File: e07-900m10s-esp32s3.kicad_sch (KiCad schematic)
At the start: 21 parts, among them J1 Conn_01x08_Pin, J2 C3/S3mini, U1 E07-900M10S, U2 ESP32-S3-DevKitC

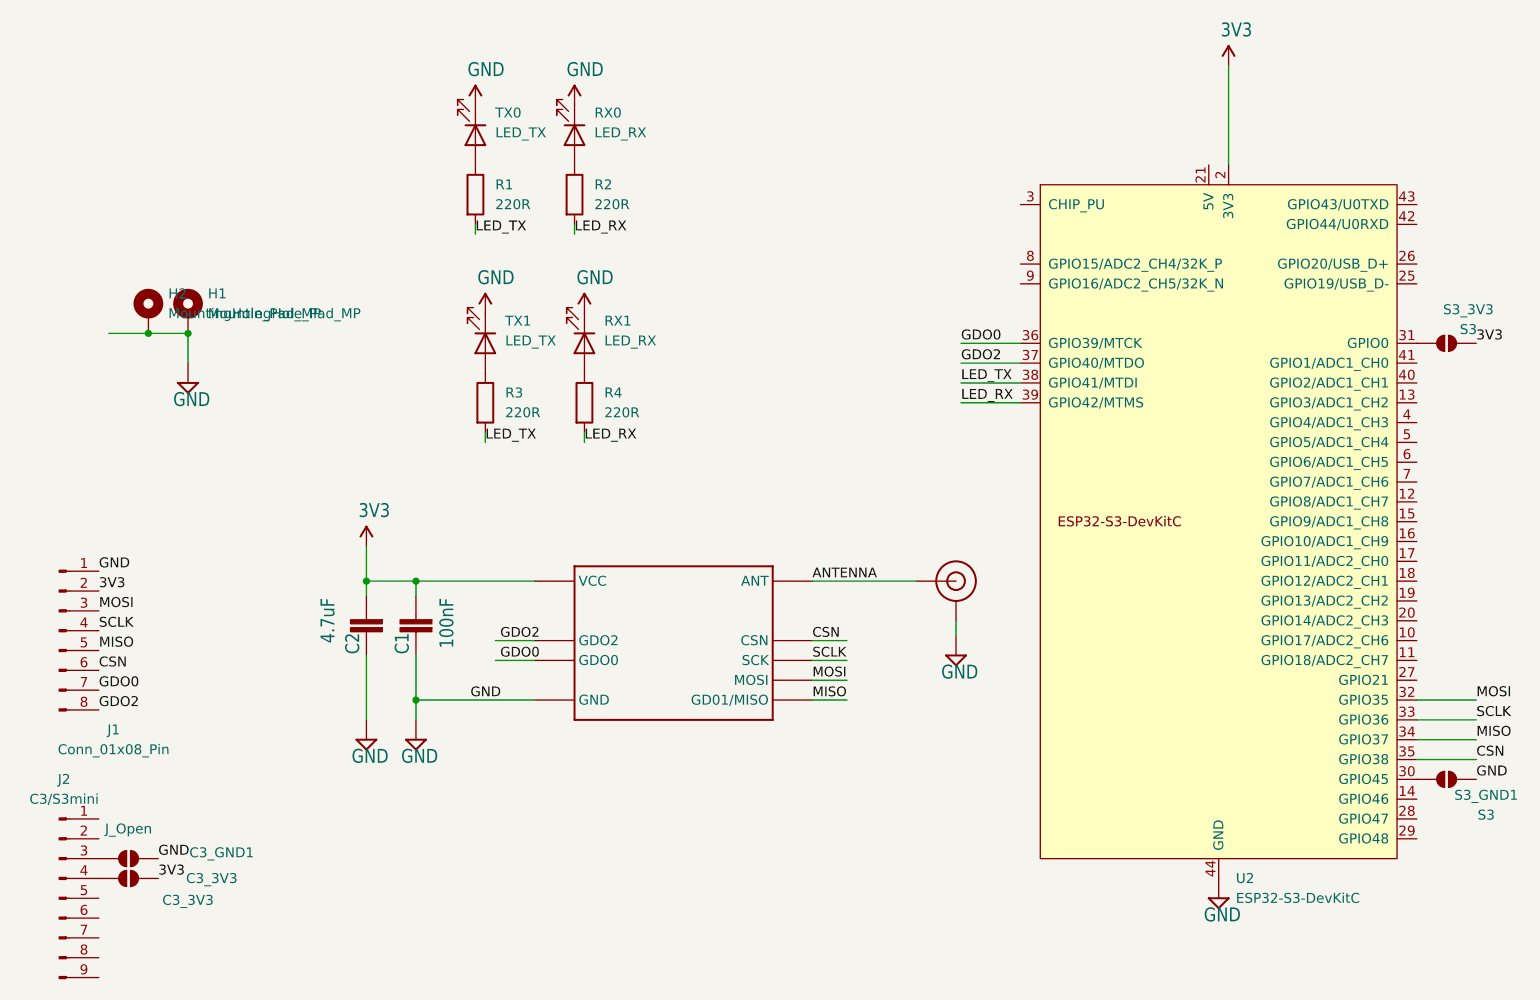
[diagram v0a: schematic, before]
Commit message: New version for JLC production
Header removed, PCB extended LED's switched for standard basic part and added MPN to components JLC solders.
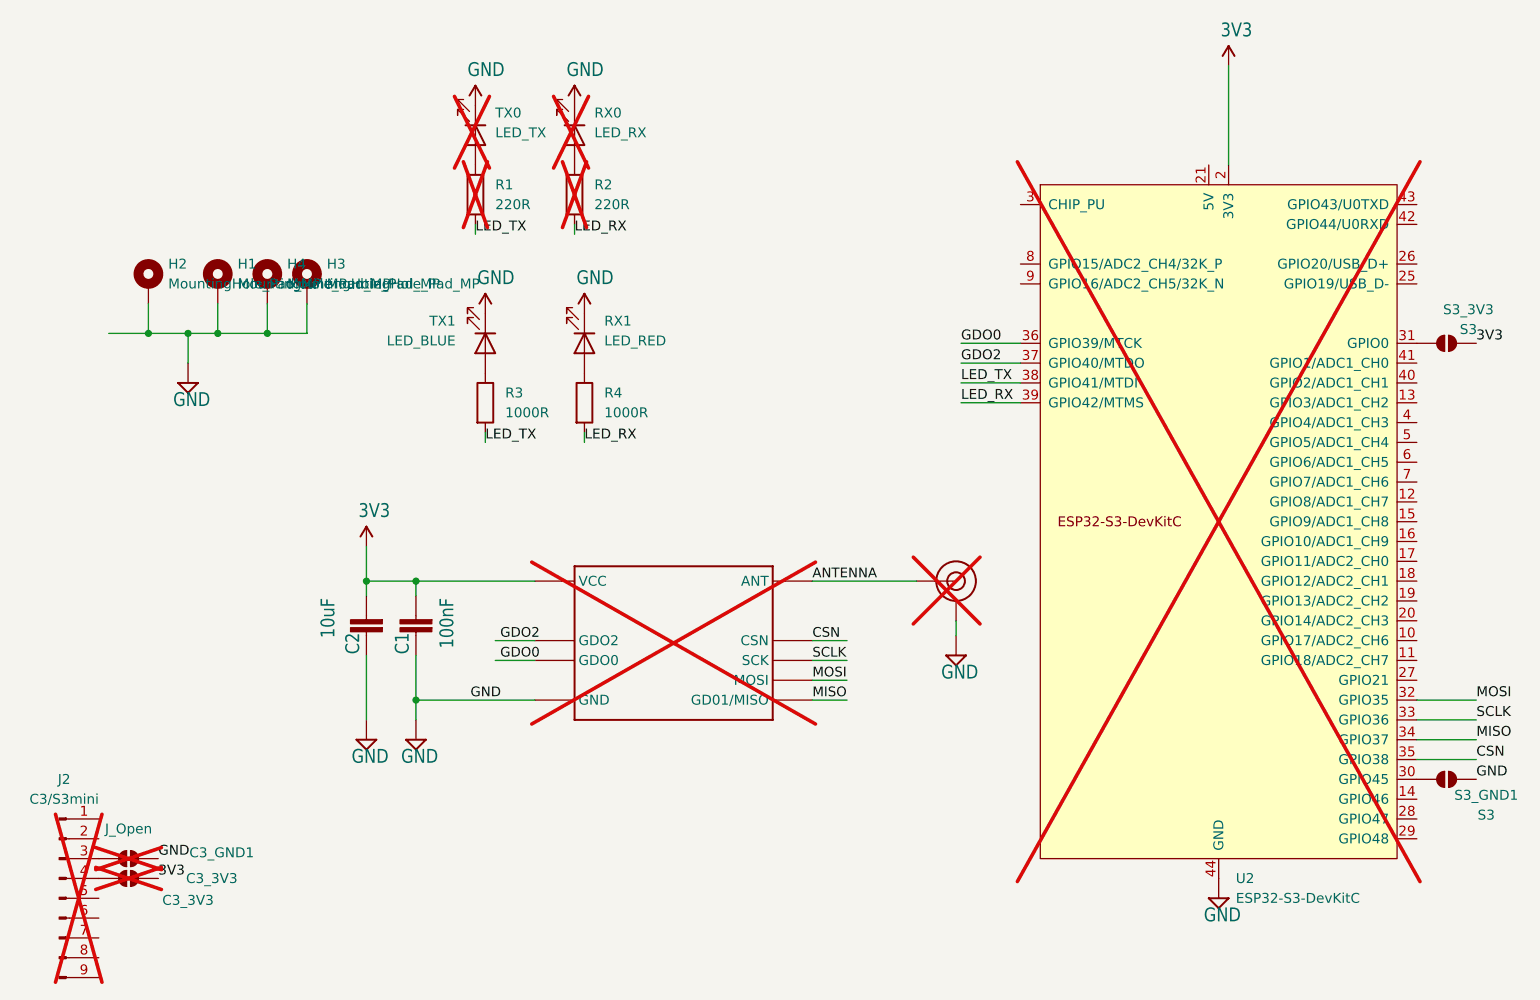
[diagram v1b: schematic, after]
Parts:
- removed J1: Conn_01x08_Pin, Connector_PinHeader_2.54mm:PinHeader_1x08_P2.54mm_Vertical, symbol Connector:Conn_01x08_Pin
- added H3, H4: MountingHole_Pad_MP, MountingHole:MountingHole_2.5mm_Pad_Via, symbol Mechanical:MountingHole_Pad_MP
- C1: MPN (none) -> C24497
- C2: value 4.7uF -> 10uF; MPN (none) -> C13585
- C3_3V3, C3_GND1, J$1, J2: now not fitted
- R1, R2, RX0, TX0, U1, U2: now not fitted; now left out of the parts list
- R3, R4: value 220R -> 1000R
- RX1: value LED_RX -> LED_RED; footprint LED_SMD:LED_1206_3216Metric_Pad1.42x1.75mm_HandSolder -> LED_SMD:LED_0805_2012Metric; MPN (none) -> C84256
- TX1: value LED_TX -> LED_BLUE; footprint LED_SMD:LED_1206_3216Metric_Pad1.42x1.75mm_HandSolder -> LED_SMD:LED_0805_2012Metric; MPN (none) -> C2297
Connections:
- net GND: now also H3.MP, H4.MP
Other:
- moved on the sheet: H1, H2
